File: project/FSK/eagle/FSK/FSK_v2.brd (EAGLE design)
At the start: 173 x 74 mm, 31 parts, among them IC1 74AUC1G32DCK, X1 SMA-142-0711-821/826, X2 SMA-142-0711-821/826, X3 SMA-142-0711-821/826, X4 SMA-142-0711-821/826, X5 SMA-142-0711-821/826, X6 22-23-2021

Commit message: updates to FSK board
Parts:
- removed LED1: S4301B, led-7-segment:S4301B
- added C4, C5: (no value), rcl:C0603
- added R11, R12, R13, R14, R15, R16, R17: (no value), rcl:R0603
- added U$11: 7S_DISPLAY, ECE532_Parts:7S_DISPLAY
- moved X6 8.01 mm to (111.7, 68.7)
- moved IC1 2.54 mm to (121.3, 44.6)
- moved R10 1.78 mm to (125.6, 46.0)
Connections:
- removed net AGND: IC1.3, U$5.12, U$5.13
- new net N$20: R14.1, U$4.10
- new net N$21: R15.1, U$4.9
- new net N$22: R16.1, U$4.15
- new net N$23: R17.1, U$4.14
- new net N$3: R11.2, U$11.10
- new net N$4: R12.2, U$11.9
- new net N$7: R13.2, U$11.6
- net GND1: now also C4.2, C5.2, IC1.3, U$11.3, U$11.8, U$5.12, U$5.13; no longer LED1.3, LED1.8
- net N$13: now also R14.2, U$11.5; no longer LED1.4, U$4.9
- net N$14: now also R15.2, U$11.4; no longer LED1.5, U$4.10
- net N$15: now also R16.2, U$11.1; no longer LED1.7, U$4.11
- net N$16: now also R17.2, U$11.2; no longer LED1.9, U$4.12
- net N$17: now also R11.1; no longer LED1.10
- net N$18: now also R12.1, U$4.12; no longer LED1.1, U$4.14
- net N$19: now also R13.1, U$4.11; no longer LED1.2, U$4.15
- net VCC: now also C4.1, C5.1
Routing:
- net N$15: track 31.9 -> 2.71 mm
- net N$16: track 30.6 -> 2.71 mm
- net N$22: track 0.00 -> 19.1 mm
- net N$21: track 0.00 -> 18.6 mm
- net N$20: track 0.00 -> 18.3 mm
- net N$23: track 0.00 -> 17.6 mm
- net N$14: track 20.3 -> 2.71 mm
- net N$13: track 17.9 -> 2.81 mm
- net AGND: track 14.7 -> 0.00 mm
- net N$4: track 0.00 -> 13.9 mm
- net N$17: track 31.5 -> 17.7 mm
- net N$3: track 0.00 -> 12.9 mm
- net N$7: track 0.00 -> 11.5 mm
- net GND1: track 15.9 -> 25.8 mm, vias 12 -> 14
- net N$19: track 30.3 -> 21.3 mm
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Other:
- board size 173 x 74 mm -> 157 x 74 mm
- board text added: "2.4GHz filter"
- board text added: "2.4GHz=0 2.6GHz=1"
- board text added: "2.6GHz filter"
- board text added: "Carlos Mariscal Cameron Tribe"

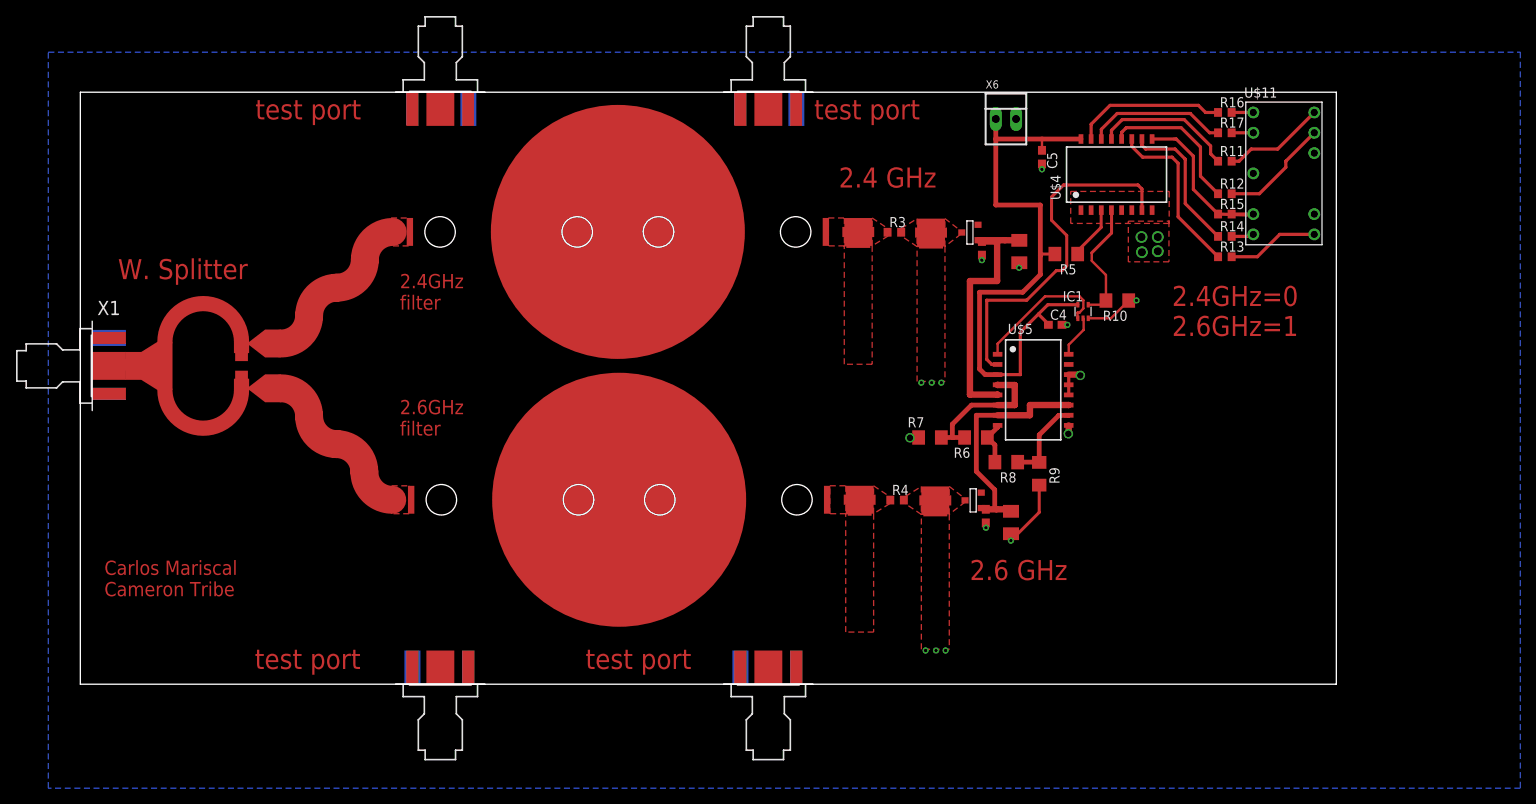
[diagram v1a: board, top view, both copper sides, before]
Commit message: fixed footprints for comp. and  SSD driver
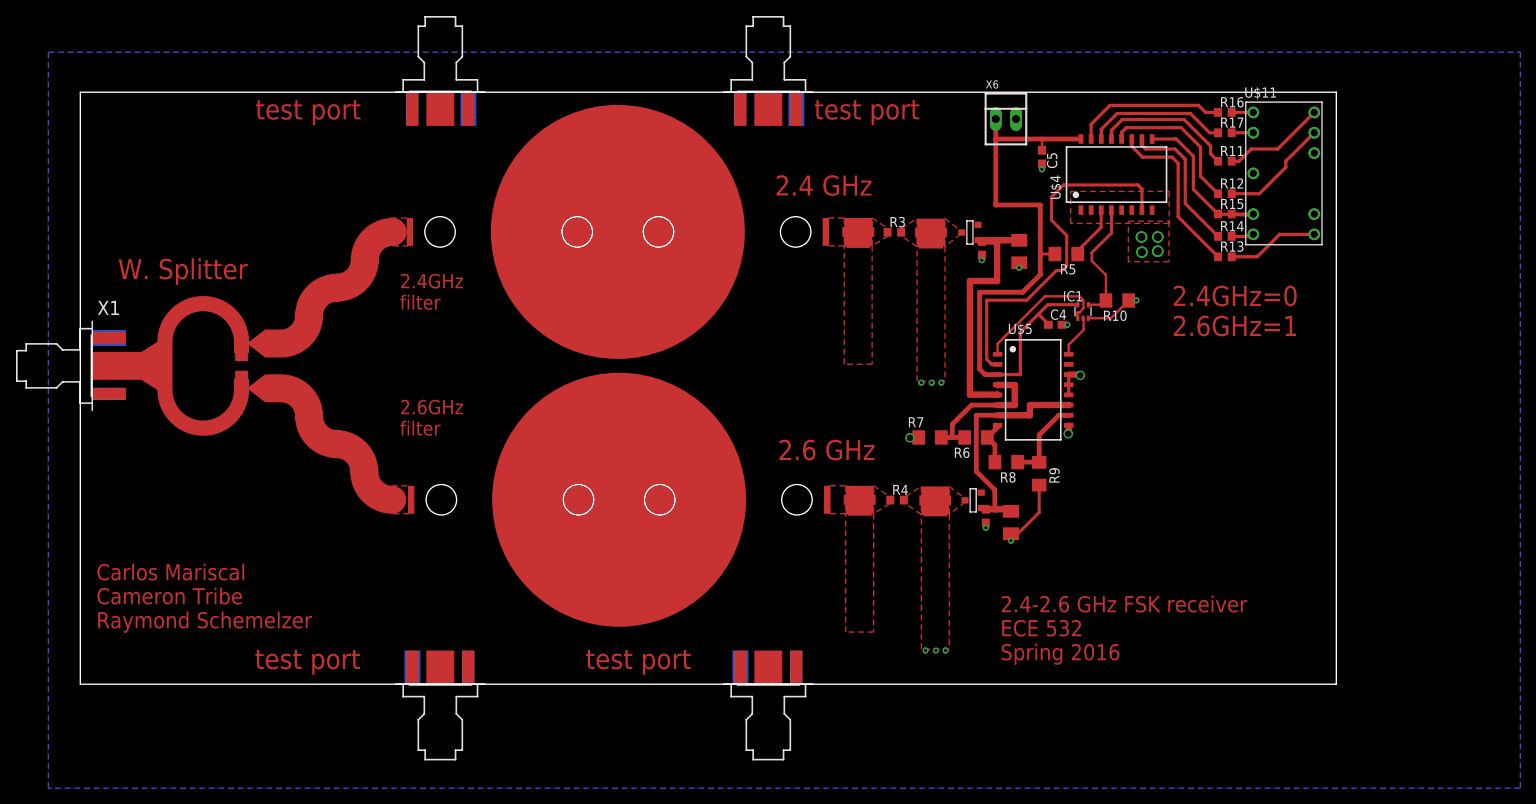
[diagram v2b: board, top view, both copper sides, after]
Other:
- board text added: "2.4-2.6 GHz FSK receiver ECE 532 Spring 2016"
- board text added: "Carlos Mariscal Cameron Tribe Raymond Schemelzer"
- board text removed: "Carlos Mariscal Cameron Tribe"
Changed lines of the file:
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@@
 <wire x1="-4" y1="72" x2="-4" y2="-2" width="0" layer="20"/>
 <text x="0.698" y="48.635" size="2.5" layer="1" font="vector" ratio="15">W. Splitter</text>
-<text x="90.8035125" y="60.083053125" size="2.5" layer="1" font="vector" ratio="15">2.4 GHz</text>
-<text x="107.178" y="11.019784375" size="2.5" layer="1" font="vector" ratio="15">2.6 GHz</text>
+<text x="82.8035125" y="59.083053125" size="2.5" layer="1" font="vector" ratio="15">2.4 GHz</text>
+<text x="83.178" y="26.019784375" size="2.5" layer="1" font="vector" ratio="15">2.6 GHz</text>
 <text x="87.72100625" y="68.6" size="2.5" layer="1" ratio="15" distance="55">test port</text>
 <text x="17.87100625" y="68.6" size="2.5" layer="1" ratio="15" distance="55">test port</text>
@@
 <text x="35.941" y="44.831" size="1.778" layer="1" ratio="15">2.4GHz
 filter</text>
-<text x="-1" y="9" size="1.778" layer="1">Carlos Mariscal
-Cameron Tribe</text>
+<text x="-2" y="5" size="2" layer="1" ratio="10">Carlos Mariscal
+Cameron Tribe
+Raymond Schemelzer</text>
+<text x="111" y="1" size="2" layer="1" ratio="10">2.4-2.6 GHz FSK receiver
+ECE 532
+Spring 2016</text>
 </plain>
 <attributes>
